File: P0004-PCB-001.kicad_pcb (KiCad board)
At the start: 2 copper layers, 63.5 x 38.5 mm, 104 parts, among them CN1 104031-0811, CN2 Liansheng PH--00603, CN3 Molex 105057-0001, CN4 Samtec FTSH-107-01-L-DV-K, CN5 M20-9990346, SW1 Khon TSB06331-090D332DA-R0500, SW2 Khon TSB06331-090D332DA-R0500, SW3 Khon TSB06331-090D332DA-R0500, SW4 Khon TSB06331-090D332DA-R0500, U1 W5500, U2 TMP102AIDRL, U3 Microchip 24AA256UIDT-I/ST, U4 STM32H743VIT6, U5 TI LMR54410DBV, U6 TI TPS2553DBV, U7 TI LMR54410DBV

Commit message: did a few little bits on layout
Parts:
- removed C20, C22, C23: 47u, Capacitor_SMD:C_1206_3216Metric
- added C35: 22u, Capacitor_SMD:C_0603_1608Metric, F.Cu at (201.5, 94.5)
- added C36: 22u, Capacitor_SMD:C_0603_1608Metric, F.Cu at (201.5, 96.0)
- added C37: 22u, Capacitor_SMD:C_0603_1608Metric, F.Cu at (201.5, 97.5)
- added C38: 22u, Capacitor_SMD:C_0603_1608Metric, F.Cu at (201.5, 99.0)
- moved D13 28.0 mm to (202.2, 116.5)
- moved FB1 26.0 mm to (190.5, 111.2)
- moved U2 23.4 mm to (193.8, 77.2)
- moved D12 6.97 mm to (203.8, 101.5)
- moved C9 3.36 mm to (180.8, 111.5)
- moved C6 2.70 mm to (189.5, 103.0), turned to -90 degrees
- moved C7 2.70 mm to (183.2, 113.5), turned to -90 degrees
- moved R3 2.00 mm to (181.0, 101.0), turned to 0 degrees
- moved R4 1.58 mm to (180.5, 102.5), turned to -90 degrees
- moved F3 1.27 mm to (201.0, 118.0), turned to 0 degrees
- moved C4 0.56 mm to (190.5, 103.0), turned to -90 degrees
- moved C1 0.51 mm to (184.5, 97.5)
- moved XT1 0.51 mm to (184.5, 99.5)
- moved C2 0.50 mm to (182.5, 99.5)
- moved R1 0.50 mm to (185.0, 101.5)
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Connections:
- CN3 pad 4: unconnected-(CN3-GND-Pad4) -> 0V
- D12 pad 2: unconnected-(D12-GND-Pad2) -> 0V
- D12 pad 5: unconnected-(D12-VBUS-Pad5) -> 5V_VBUS
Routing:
- net 3V3: track 0.00 -> 19.9 mm, vias 0 -> 8
- net /Microcontroller/SWD_SWDIO: track 0.00 -> 13.1 mm
- net /Microcontroller/DEBUG_UART_RX: track 2.25 -> 14.5 mm, vias 1 -> 2
- net 0V: track 17.3 -> 28.2 mm, vias 1 -> 47
- net /Microcontroller/DEBUG_UART_TX: track 2.25 -> 12.9 mm, vias 1 -> 2
- net /Ethernet/PHY_VDDA: track 4.42 -> 12.5 mm
- net /Microcontroller/SWD_SWCLK: track 0.00 -> 7.77 mm
- net /Power Supplies/VOUT_5V: track 0.00 -> 4.28 mm
- net 5V: track 0.00 -> 4.18 mm
- net /Power Supplies/VOUT_3V3: track 6.14 -> 2.51 mm
- net Net-(U1-TXP): track 0.00 -> 3.20 mm
- net Net-(U6-ILIM): track 0.00 -> 3.04 mm
- net /Microcontroller/SWD_SWO: track 0.00 -> 2.94 mm
- net /Microcontroller/~{SWD_NRST}: track 0.00 -> 2.93 mm
- net /Ethernet/ETH_TX_P: track 0.00 -> 2.92 mm
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- added copper zone on F.Cu, net /Ethernet/PHY_VDDA
- added copper zone on F.Cu, net /Power Supplies/SW_3V3
- added copper zone on F.Cu, net /Power Supplies/VIN_SAFE
- added copper zone on F.Cu, net 0V
- added copper zone on In1.Cu, net 0V
- added copper zone on In2.Cu, net 0V
- added copper zone on F.Cu, net 3V3
- added copper zone on B.Cu, net 5V_VBUS
- added copper zone on F.Cu, net 5V_VBUS
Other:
- copper layers 2 -> 4

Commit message: more progress
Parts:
- removed the CN3 at (204.0, 101.5)
- removed the D1 at (136.2, 98.0)
- removed the D12 at (203.8, 101.5)
- added C17: 4u7, Capacitor_WUT:C_0402_1005Metric, F.Cu at (167.5, 114.2)
- added C18: 100n, Capacitor_WUT:C_0402_1005Metric, F.Cu at (162.0, 103.2)
- added C19: 100n, Capacitor_WUT:C_0402_1005Metric, F.Cu at (165.5, 114.2)
- added C20: 100n, Capacitor_WUT:C_0402_1005Metric, F.Cu at (177.0, 114.2)
- added C21: 100n, Capacitor_WUT:C_0402_1005Metric, F.Cu at (180.5, 98.8)
- added C22: 100n, Capacitor_WUT:C_0402_1005Metric, F.Cu at (161.2, 101.5)
- added C23: 100n, Capacitor_WUT:C_0402_1005Metric, F.Cu at (165.5, 95.8)
- added C24: 100n, Capacitor_WUT:C_0402_1005Metric, F.Cu at (162.0, 108.0)
- added C25: 2u2, Capacitor_WUT:C_0402_1005Metric, F.Cu at (181.0, 100.2)
- added C26: 2u2, Capacitor_WUT:C_0402_1005Metric, F.Cu at (161.0, 108.0)
- added C27: 2u2, Capacitor_WUT:C_0402_1005Metric, F.Cu at (175.0, 114.2)
- added C28: 100n, Capacitor_WUT:C_0402_1005Metric, F.Cu at (162.0, 110.0)
- added C29: 100n, Capacitor_WUT:C_0402_1005Metric, F.Cu at (161.5, 106.5)
- added CN5: Molex 105057-0001, Connector_WUT:USB-A_Molex_105057-0001_TH_Vertical, B.Cu at (204.0, 101.5)
- added D10: USBLC6-2P6, Package_TO_SOT_SMD:SOT-666, F.Cu at (203.8, 101.5)
- added F1: 1A, Fuse:Fuse_0603_1608Metric, F.Cu at (186.0, 86.8)
- added FB3: 1k8, Inductor_SMD:L_0402_1005Metric, F.Cu at (161.0, 110.0)
- added R10: 10k, Resistor_WUT:R_0402_1005Metric, F.Cu at (169.8, 95.5)
- added R23: 1k0, Resistor_WUT:R_0402_1005Metric, F.Cu at (200.8, 88.8)
- added R24: 1k0, Resistor_WUT:R_0402_1005Metric, F.Cu at (200.8, 90.8)
- added R25: 1k0, Resistor_WUT:R_0402_1005Metric, F.Cu at (200.8, 92.8)
- added R26: 33R, Resistor_WUT:R_0402_1005Metric, F.Cu at (161.2, 97.5)
- added R27: 33R, Resistor_WUT:R_0402_1005Metric, F.Cu at (161.2, 100.5)
- added R28: 33R, Resistor_WUT:R_0402_1005Metric, F.Cu at (161.2, 95.5)
- added R29: 33R, Resistor_WUT:R_0402_1005Metric, F.Cu at (161.2, 96.5)
- added R30: 33R, Resistor_WUT:R_0402_1005Metric, F.Cu at (161.2, 99.5)
- added R31: 33R, Resistor_WUT:R_0402_1005Metric, F.Cu at (161.2, 98.5)
- added R32: 1k0, Resistor_WUT:R_0402_1005Metric, F.Cu at (195.8, 103.5)
- added R33: 1k0, Resistor_WUT:R_0402_1005Metric, F.Cu at (193.8, 103.5)
- added R34: 1k0, Resistor_WUT:R_0402_1005Metric, F.Cu at (194.8, 103.5)
- R4: value 10k -> 1k0
- moved C16 25.1 mm to (186.0, 88.2)
- moved R18 17.4 mm to (198.8, 102.8), turned to 0 degrees
- moved R4 12.3 mm to (192.8, 103.5)
- moved C9 3.20 mm to (182.8, 114.0), turned to 180 degrees
- moved D1 3.00 mm to (185.2, 92.2), turned to -90 degrees
- moved R3 2.11 mm to (183.0, 101.5), turned to 180 degrees
- moved R7 1.77 mm to (179.2, 113.8), turned to -90 degrees
- moved C15 1.50 mm to (185.2, 90.0), turned to 90 degrees
- moved R6 1.06 mm to (180.2, 113.8), turned to -90 degrees
- moved R9 1.00 mm to (185.2, 94.5)
- moved C7 0.71 mm to (182.8, 113.0), turned to 180 degrees
- moved D13 0.71 mm to (197.0, 103.5), turned to 90 degrees
- moved R15 0.71 mm to (161.5, 105.5), turned to 0 degrees
- renumbered C27 to C15, C32 to C16, C34 to C30, C28 to C31, C15 to C32, C29 to C33, C19 to C34, C36 to C35, C35 to C36, C30 to C37, C21 to C38, C37 to C39, C31 to C40, C25 to C41, C38 to C42, C33 to C43, C26 to C44, CN2 to CN1, CN4 to CN2, CN1 to CN3, CN5 to CN4, D11 to D1, D2 to D11, D13 to D12, D14 to D13, D9 to D2, D10 to D3, D7 to D4, D8 to D5, D3 to D6, D5 to D7, D4 to D8, D6 to D9, F1 to F2, F2 to F4, L2 to L1, L1 to L2, R20 to R11, R21 to R12, R18 to R13, R19 to R14, R23 to R15, R10 to R16, R9 to R17, R11 to R18, R29 to R19, R30 to R20, R15 to R21, R16 to R22, R22 to R9, U4 to U2, U2 to U3, U3 to U4, U7 to U5, U5 to U6, U6 to U7
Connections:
- C16 pad 1: /Power Supplies/VIN_SAFE -> Net-(CN3-VDD)
- CN3 pad 1: Net-(CN1-DAT2) -> /Microcontroller/SDMMC_D2
- CN3 pad 10: unconnected-(CN1-DET_A-Pad10) -> /Microcontroller/~{SD_CARD_DET}
- CN3 pad 11: unconnected-(CN1-SHIELD-Pad11) -> 0V
- CN3 pad 2: Net-(CN1-DAT3/CD) -> /Microcontroller/SDMMC_D3
- CN3 pad 3: Net-(CN1-CMD) -> /Microcontroller/SDMMC_CMD
- CN3 pad 4: unconnected-(CN1-VDD-Pad4) -> Net-(CN3-VDD)
- CN3 pad 5: Net-(CN1-CLK) -> /Microcontroller/SDMMC_CLK
- CN3 pad 6: unconnected-(CN1-VSS-Pad6) -> 0V
- CN3 pad 7: Net-(CN1-DAT0) -> /Microcontroller/SDMMC_D0
- CN3 pad 8: Net-(CN1-DAT1) -> /Microcontroller/SDMMC_D1
- CN3 pad 9: unconnected-(CN1-DET_B-Pad9) -> 0V
- LD1 pad 1: unconnected-(LD1-R-Pad1) -> Net-(LD1-R)
- LD1 pad 2: unconnected-(LD1-G-Pad2) -> Net-(LD1-G)
- LD1 pad 3: unconnected-(LD1-B-Pad3) -> Net-(LD1-B)
- LD1 pad 4: unconnected-(LD1-A-Pad4) -> 3V3
- R16 pad 1: /Power Supplies/VBUS_EN -> /Microcontroller/USB_VBUS_EN
- R18 pad 2: /Power Supplies/~{VBUS_FAULT} -> /Microcontroller/~{USB_VBUS_FAULT}
- R4 pad 2: /Ethernet/~{ETH_PHY_RST} -> Net-(R33-Pad1)
- U2 pad 100: unconnected-(U4-VDD-Pad100) -> 3V3
- U2 pad 11: unconnected-(U4-VDD-Pad11) -> 3V3
- U2 pad 16: /Microcontroller/ETH_PHY_MOSI -> /Ethernet/MOSI
- U2 pad 17: /Microcontroller/ETH_PHY_MISO -> /Ethernet/MISO
- U2 pad 20: unconnected-(U4-VREF+-Pad20) -> /Microcontroller/VDDA
- U2 pad 21: unconnected-(U4-VDDA-Pad21) -> /Microcontroller/VDDA
- U2 pad 27: unconnected-(U4-VDD-Pad27) -> 3V3
- U2 pad 48: unconnected-(U4-VCAP-Pad48) -> Net-(C25-Pad1)
- U2 pad 50: unconnected-(U4-VDD-Pad50) -> 3V3
- U2 pad 51: /Microcontroller/~{ETH_PHY_CS} -> /Ethernet/~{CS}
- U2 pad 52: /Microcontroller/ETH_PHY_SCK -> /Ethernet/SCLK
- U2 pad 6: unconnected-(U4-VBAT-Pad6) -> 3V3
- U2 pad 61: unconnected-(U4-PD14-Pad61) -> /Microcontroller/USB_VBUS_EN
- U2 pad 62: unconnected-(U4-PD15-Pad62) -> /Microcontroller/~{USB_VBUS_FAULT}
- U2 pad 63: unconnected-(U4-PC6-Pad63) -> /Ethernet/~{ETH_PHY_RST}
- U2 pad 64: unconnected-(U4-PC7-Pad64) -> /Ethernet/~{ETH_PHY_INT}
- U2 pad 67: /Microcontroller/RGB_R -> /Microcontroller/RGB_G
- U2 pad 68: /Microcontroller/RGB_G -> /Microcontroller/RGB_B
- U2 pad 69: /Microcontroller/RGB_B -> /Microcontroller/RGB_R
- U2 pad 73: unconnected-(U4-VCAP-Pad73) -> Net-(C25-Pad1)
- U2 pad 75: unconnected-(U4-VDD-Pad75) -> 3V3
- U2 pad 83: unconnected-(U4-PD2-Pad83) -> /Microcontroller/SDMMC_CMD
- U2 pad 90: unconnected-(U4-PB4-Pad90) -> /Microcontroller/~{SD_CARD_DET}
- U7 pad 3: /Power Supplies/VBUS_EN -> /Microcontroller/USB_VBUS_EN
- U7 pad 4: /Power Supplies/~{VBUS_FAULT} -> /Microcontroller/~{USB_VBUS_FAULT}
- ZF1 pad 3: unconnected-(ZF1-SCL-Pad3) -> Net-(ZF1-SCL)
- ZF1 pad 4: unconnected-(ZF1-SDA-Pad4) -> Net-(ZF1-SDA)
- ZF1 pad 5: unconnected-(ZF1-RES-Pad5) -> Net-(ZF1-RES)
- ZF1 pad 6: unconnected-(ZF1-DC-Pad6) -> Net-(ZF1-DC)
- ZF1 pad 7: unconnected-(ZF1-~{CS}-Pad7) -> Net-(ZF1-~{CS})
- ZF1 pad 8: unconnected-(ZF1-BLK-Pad8) -> Net-(ZF1-BLK)
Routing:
- net /Microcontroller/USB_HOST_D_P: track 0.00 -> 41.4 mm, vias 0 -> 2
- net /Microcontroller/SDMMC_D0: track 0.00 -> 40.0 mm, vias 0 -> 2
- net /Microcontroller/USB_HOST_D_N: track 0.00 -> 39.1 mm, vias 0 -> 2
- net 0V: track 28.2 -> 66.7 mm, vias 47 -> 110
- net /Microcontroller/SDMMC_D1: track 0.00 -> 38.2 mm, vias 0 -> 2
- net /Microcontroller/~{USB_VBUS_FAULT}: track 0.00 -> 35.0 mm, vias 0 -> 3
- net /Microcontroller/USB_VBUS_EN: track 0.00 -> 34.6 mm, vias 0 -> 2
- net /Microcontroller/RGB_R: track 0.00 -> 34.3 mm, vias 0 -> 2
- net /Microcontroller/RGB_G: track 0.00 -> 33.4 mm, vias 0 -> 2
- net /Microcontroller/SDMMC_CMD: track 0.00 -> 33.3 mm, vias 0 -> 2
- net /Microcontroller/RGB_B: track 0.00 -> 31.2 mm, vias 0 -> 2
- net /Microcontroller/SDMMC_CLK: track 0.00 -> 29.0 mm, vias 0 -> 2
- net /Microcontroller/~{SD_CARD_DET}: track 0.00 -> 26.6 mm, vias 0 -> 1
- net Net-(ZF1-SDA): track 0.00 -> 26.0 mm, vias 0 -> 1
- net Net-(ZF1-BLK): track 0.00 -> 25.5 mm, vias 0 -> 1
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- added copper zone on B.Cu, net 3V3

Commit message: most things connected
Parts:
- added C45: 10u, Capacitor_SMD:C_0603_1608Metric, F.Cu at (147.5, 92.2)
- added C46: 100n, Capacitor_WUT:C_0402_1005Metric, F.Cu at (170.0, 95.2)
- added C47: 100n, Capacitor_WUT:C_0402_1005Metric, F.Cu at (163.2, 93.8)
- added C48: 100n, Capacitor_WUT:C_0402_1005Metric, F.Cu at (166.6, 94.5)
- added CN10: JST BM06B-SRSS-TB(LF)(SN), Connector_JST:JST_SH_BM06B-SRSS-TB_1x06-1MP_P1.00mm_Vertical, F.Cu at (156.0, 108.2)
- added CN11: BM05B-SRSS-TB(LF)(SN), Connector_JST:JST_SH_BM05B-SRSS-TB_1x05-1MP_P1.00mm_Vertical, F.Cu at (149.5, 98.2)
- added CN6: BM03B-SRSS-TB(LF)(SN), Connector_JST:JST_SH_BM03B-SRSS-TB_1x03-1MP_P1.00mm_Vertical, F.Cu at (149.5, 106.8)
- added CN7: BM04B-SRSS-TB(LF)(SN), Connector_JST:JST_SH_BM04B-SRSS-TB_1x04-1MP_P1.00mm_Vertical, F.Cu at (159.0, 89.5)
- added CN8: BM04B-SRSS-TB(LF)(SN), Connector_JST:JST_SH_BM04B-SRSS-TB_1x04-1MP_P1.00mm_Vertical, F.Cu at (151.5, 89.5)
- added CN9: JST BM06B-SRSS-TB(LF)(SN), Connector_JST:JST_SH_BM06B-SRSS-TB_1x06-1MP_P1.00mm_Vertical, F.Cu at (156.0, 98.2)
- added R35: 10k, Resistor_WUT:R_0402_1005Metric, F.Cu at (169.0, 95.2)
- added R36: 33R, Resistor_WUT:R_0402_1005Metric, F.Cu at (152.8, 107.8)
- added R37: 33R, Resistor_WUT:R_0402_1005Metric, F.Cu at (152.8, 105.8)
- added R38: 33R, Resistor_WUT:R_0402_1005Metric, F.Cu at (162.8, 90.0)
- added R39: 33R, Resistor_WUT:R_0402_1005Metric, F.Cu at (162.8, 89.0)
- added R40: 33R, Resistor_WUT:R_0402_1005Metric, F.Cu at (162.8, 88.0)
- added R41: 33R, Resistor_WUT:R_0402_1005Metric, F.Cu at (155.2, 90.0)
- added R42: 33R, Resistor_WUT:R_0402_1005Metric, F.Cu at (155.2, 89.0)
- added R43: 33R, Resistor_WUT:R_0402_1005Metric, F.Cu at (155.2, 88.0)
- added R44: 33R, Resistor_WUT:R_0402_1005Metric, F.Cu at (152.8, 100.8)
- added R45: 33R, Resistor_WUT:R_0402_1005Metric, F.Cu at (152.8, 98.8)
- added R46: 33R, Resistor_WUT:R_0402_1005Metric, F.Cu at (152.8, 96.8)
- added R47: 33R, Resistor_WUT:R_0402_1005Metric, F.Cu at (152.8, 94.8)
- added R48: 33R, Resistor_WUT:R_0402_1005Metric, F.Cu at (159.2, 101.8)
- added R49: 33R, Resistor_WUT:R_0402_1005Metric, F.Cu at (159.2, 99.8)
- added R50: 33R, Resistor_WUT:R_0402_1005Metric, F.Cu at (159.2, 97.8)
- added R51: 33R, Resistor_WUT:R_0402_1005Metric, F.Cu at (159.2, 95.8)
- added R52: 33R, Resistor_WUT:R_0402_1005Metric, F.Cu at (159.8, 94.2)
- added R53: 33R, Resistor_WUT:R_0402_1005Metric, F.Cu at (159.2, 111.8)
- added R54: 33R, Resistor_WUT:R_0402_1005Metric, F.Cu at (159.2, 109.8)
- added R55: 33R, Resistor_WUT:R_0402_1005Metric, F.Cu at (159.2, 107.8)
- added R56: 33R, Resistor_WUT:R_0402_1005Metric, F.Cu at (159.2, 105.8)
- added R57: 33R, Resistor_WUT:R_0402_1005Metric, F.Cu at (159.8, 104.2)
- moved U3 33.9 mm to (163.2, 92.0), turned to -90 degrees
- moved R10 1.77 mm to (168.0, 95.2), turned to -90 degrees
- moved CN4 0.29 mm to (169.8, 87.2)
- moved U4 0.26 mm to (166.1, 90.0), turned to -90 degrees
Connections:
- CN5 pad 5: unconnected-(CN5-Shield-Pad5) -> 0V
- U2 pad 25: unconnected-(U2-PA3-Pad25) -> /Microcontroller/SPKR
- U2 pad 51: /Ethernet/~{CS} -> /Microcontroller/~{I2C2_ALERT}
- U2 pad 58: unconnected-(U2-PD11-Pad58) -> /Microcontroller/~{INT_ALERT}
- U2 pad 90: /Microcontroller/~{SD_CARD_DET} -> unconnected-(U2-PB4-Pad90)
- U2 pad 91: unconnected-(U2-PB5-Pad91) -> /Microcontroller/~{I2C1_ALERT}
- U2 pad 92: unconnected-(U2-PB6-Pad92) -> /Microcontroller/I2C1_SCL
- U2 pad 94: unconnected-(U2-BOOT0-Pad94) -> /Microcontroller/DFU_EN
- U2 pad 95: /Microcontroller/I2C1_SCL -> /Microcontroller/~{SD_CARD_DET}
- U2 pad 96: unconnected-(U2-PB9-Pad96) -> /Ethernet/~{CS}
- U3 pad 1: unconnected-(U3-SCL-Pad1) -> /Microcontroller/INT_SCL
- U3 pad 2: unconnected-(U3-GND-Pad2) -> 0V
- U3 pad 3: unconnected-(U3-~{ALERT}-Pad3) -> /Microcontroller/~{INT_ALERT}
- U3 pad 4: unconnected-(U3-ADD0-Pad4) -> 0V
- U3 pad 5: unconnected-(U3-V+-Pad5) -> 3V3
- U3 pad 6: unconnected-(U3-SDA-Pad6) -> /Microcontroller/INT_SDA
- U4 pad 1: unconnected-(U4-A0-Pad1) -> 0V
- U4 pad 2: unconnected-(U4-A1-Pad2) -> 0V
- U4 pad 3: unconnected-(U4-A2-Pad3) -> 0V
- U4 pad 4: unconnected-(U4-VSS-Pad4) -> 0V
- U4 pad 5: unconnected-(U4-SDA-Pad5) -> /Microcontroller/INT_SDA
- U4 pad 6: unconnected-(U4-SCL-Pad6) -> /Microcontroller/INT_SCL
- U4 pad 8: unconnected-(U4-VCC-Pad8) -> 3V3
- ZF1 pad 1: unconnected-(ZF1-GND-Pad1) -> 0V
- ZF1 pad 2: unconnected-(ZF1-VCC-Pad2) -> 3V3
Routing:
- net /Microcontroller/SPI6_MOSI: track 0.00 -> 50.4 mm, vias 0 -> 2
- net /Microcontroller/SPI6_MISO: track 0.00 -> 45.2 mm, vias 0 -> 2
- net /Microcontroller/~{I2C2_ALERT}: track 0.00 -> 41.1 mm, vias 0 -> 2
- net /Microcontroller/~{SPI6_CS}: track 0.00 -> 39.9 mm, vias 0 -> 2
- net /Microcontroller/SPI6_SCLK: track 0.00 -> 38.8 mm, vias 0 -> 2
- net /Microcontroller/I2C2_SDA: track 0.00 -> 37.3 mm, vias 0 -> 2
- net /Microcontroller/I2C2_SCL: track 0.00 -> 35.0 mm, vias 0 -> 2
- net /Microcontroller/~{INT_ALERT}: track 0.00 -> 29.1 mm, vias 0 -> 2
- net 0V: track 66.7 -> 95.3 mm, vias 110 -> 138
- net /Microcontroller/UART4_RX: track 1.63 -> 25.8 mm, vias 1 -> 2
- net /Ethernet/~{CS}: track 13.8 -> 34.4 mm
- net /Microcontroller/UART4_TX: track 1.43 -> 21.1 mm, vias 1 -> 2
- net /Microcontroller/SPKR: track 0.00 -> 16.4 mm
- net /Microcontroller/~{I2C1_ALERT}: track 0.00 -> 16.2 mm, vias 0 -> 2
- net /Microcontroller/I2C1_SDA: track 0.00 -> 15.6 mm, vias 0 -> 2
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
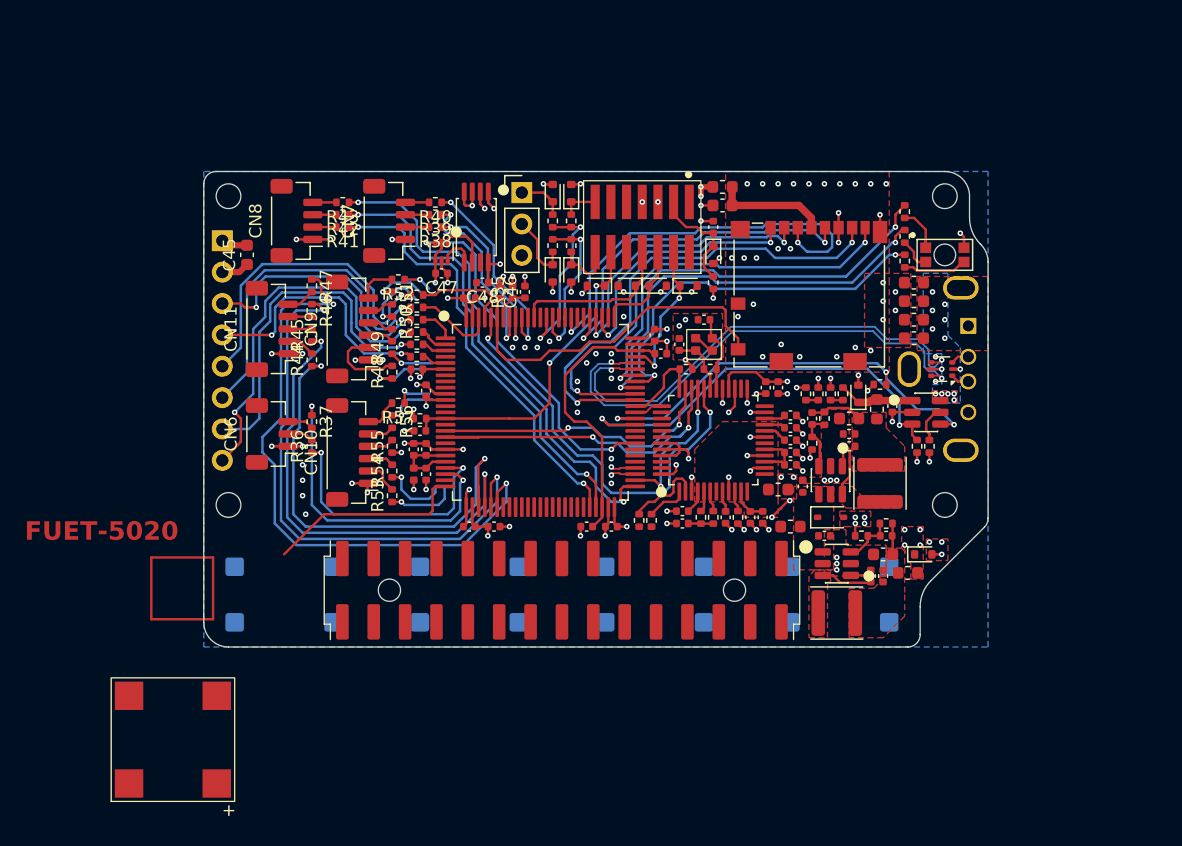
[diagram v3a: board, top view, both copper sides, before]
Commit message: headers now connected
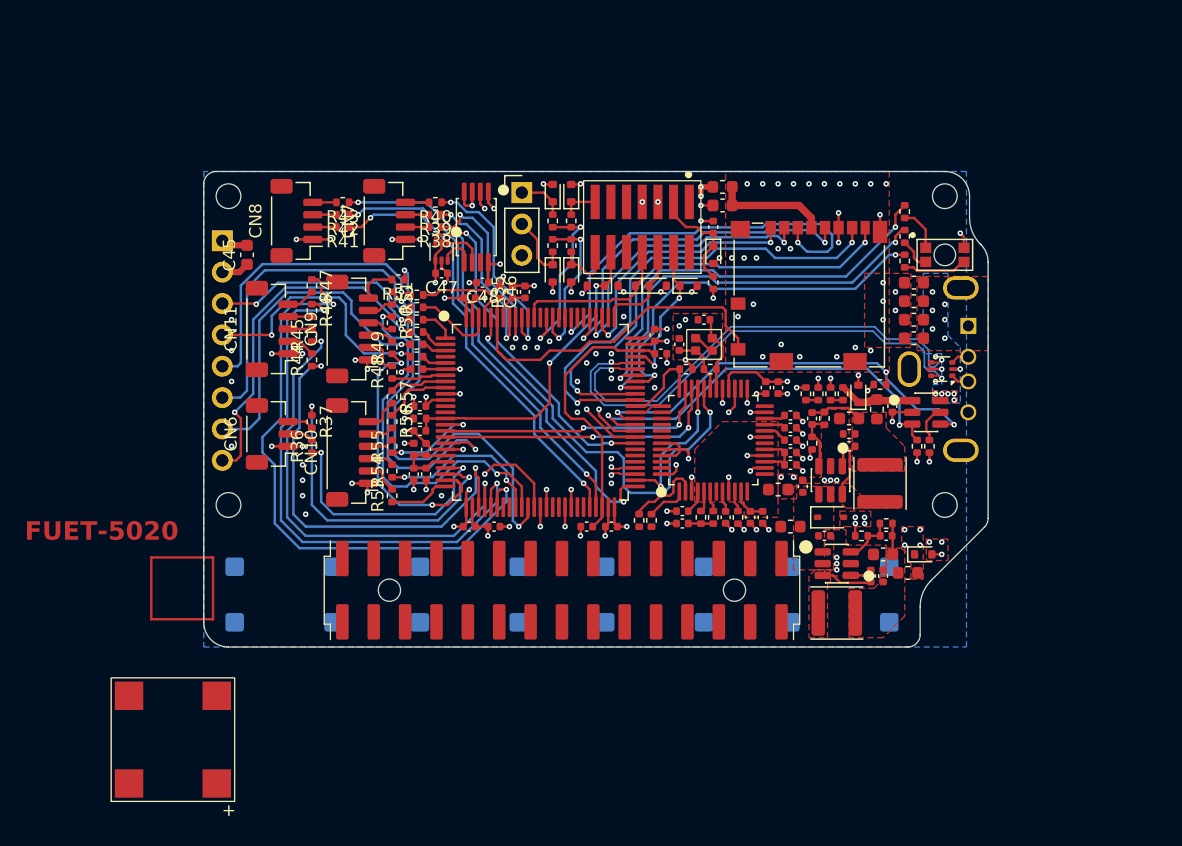
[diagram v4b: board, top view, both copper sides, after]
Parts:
- moved C26 2.00 mm to (161.0, 110.0), turned to -90 degrees
- moved FB3 2.00 mm to (161.0, 108.0), turned to 90 degrees
- moved C18 1.35 mm to (161.5, 104.5), turned to 180 degrees
- moved R57 0.71 mm to (159.2, 103.8), turned to -90 degrees
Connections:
- R48 pad 1: unconnected-(R48-Pad1) -> /Microcontroller/PC13
- R49 pad 1: unconnected-(R49-Pad1) -> /Microcontroller/PA2
- R50 pad 1: unconnected-(R50-Pad1) -> /Microcontroller/PB1
- R51 pad 1: unconnected-(R51-Pad1) -> /Microcontroller/PC3
- R52 pad 1: unconnected-(R52-Pad1) -> /Microcontroller/PB2
- R53 pad 1: unconnected-(R53-Pad1) -> /Microcontroller/PA3
- R54 pad 1: unconnected-(R54-Pad1) -> /Microcontroller/PB0
- R55 pad 1: unconnected-(R55-Pad1) -> /Microcontroller/PC0
- R56 pad 1: unconnected-(R56-Pad1) -> /Microcontroller/PC15
- R57 pad 1: unconnected-(R57-Pad1) -> /Microcontroller/PC14
- U2 pad 15: unconnected-(U2-PC0-Pad15) -> /Microcontroller/PC0
- U2 pad 18: unconnected-(U2-PC3_C-Pad18) -> /Microcontroller/PC3
- U2 pad 24: unconnected-(U2-PA2-Pad24) -> /Microcontroller/PA2
- U2 pad 25: /Microcontroller/SPKR -> /Microcontroller/PA3
- U2 pad 34: unconnected-(U2-PB0-Pad34) -> /Microcontroller/PB0
- U2 pad 35: unconnected-(U2-PB1-Pad35) -> /Microcontroller/PB1
- U2 pad 36: unconnected-(U2-PB2-Pad36) -> /Microcontroller/PB2
- U2 pad 7: unconnected-(U2-PC13-Pad7) -> /Microcontroller/PC13
- U2 pad 8: unconnected-(U2-PC14-Pad8) -> /Microcontroller/PC14
- U2 pad 9: unconnected-(U2-PC15-Pad9) -> /Microcontroller/PC15
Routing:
- net /Microcontroller/PB2: track 0.00 -> 35.5 mm, vias 0 -> 2
- net /Microcontroller/PB1: track 0.00 -> 31.0 mm, vias 0 -> 2
- net /Microcontroller/PC3: track 0.00 -> 26.3 mm, vias 0 -> 2
- net /Microcontroller/PA2: track 0.00 -> 24.1 mm, vias 0 -> 2
- net /Microcontroller/SPKR: track 16.4 -> 0.00 mm
- net /Microcontroller/PB0: track 0.00 -> 13.7 mm, vias 0 -> 2
- net /Microcontroller/PC0: track 0.00 -> 8.11 mm, vias 0 -> 2
- net unconnected-(U2-PE7-Pad37): track 0.00 -> 6.86 mm, vias 0 -> 1
- net /Microcontroller/PC15: track 0.00 -> 5.69 mm
- net unconnected-(R53-Pad1): track 5.56 -> 0.00 mm, vias 1 -> 0
- net unconnected-(R54-Pad1): track 5.52 -> 0.00 mm, vias 1 -> 0
- net unconnected-(R50-Pad1): track 5.42 -> 0.00 mm, vias 1 -> 0
- net unconnected-(R48-Pad1): track 5.06 -> 0.00 mm, vias 1 -> 0
- net /Microcontroller/PA3: track 0.00 -> 4.99 mm
- net /Microcontroller/PC14: track 0.00 -> 4.63 mm
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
